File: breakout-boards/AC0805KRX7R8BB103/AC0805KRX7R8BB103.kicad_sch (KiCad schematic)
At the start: 0 parts

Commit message: feat: create schematic for 10nf breakout board
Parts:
- added C1, C10, C11, C12, C2, C3, C4, C5, C6, C7, C8, C9: 10nF, CAPC2012X95N, symbol FixedWing:AC0805KRX7R8BB103
- added TP1, TP10, TP11, TP12, TP13, TP14, TP15, TP16, TP17, TP18, TP19, TP2, TP20, TP21, TP22, TP23, TP24, TP3, TP4, TP5, TP6, TP7, TP8, TP9: TestPoint, symbol Connector:TestPoint
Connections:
- new net: C9.2, TP21.1
- new net: C12.1, TP12.1
- new net: C6.2, TP18.1
- new net: C7.2, TP19.1
- new net: C6.1, TP6.1
- new net: C5.1, TP5.1
- new net: C5.2, TP17.1
- new net: C7.1, TP7.1
- new net: C11.2, TP23.1
- new net: C12.2, TP24.1
- new net: C4.1, TP4.1
- new net: C4.2, TP16.1
- new net: C10.2, TP22.1
- new net: C10.1, TP10.1
- new net: C2.1, TP2.1
- new net: C2.2, TP14.1
- new net: C1.2, TP13.1
- new net: C3.2, TP15.1
- new net: C1.1, TP1.1
- new net: C9.1, TP9.1
- new net: C11.1, TP11.1
- new net: C3.1, TP3.1
- new net: C8.1, TP8.1
- new net: C8.2, TP20.1

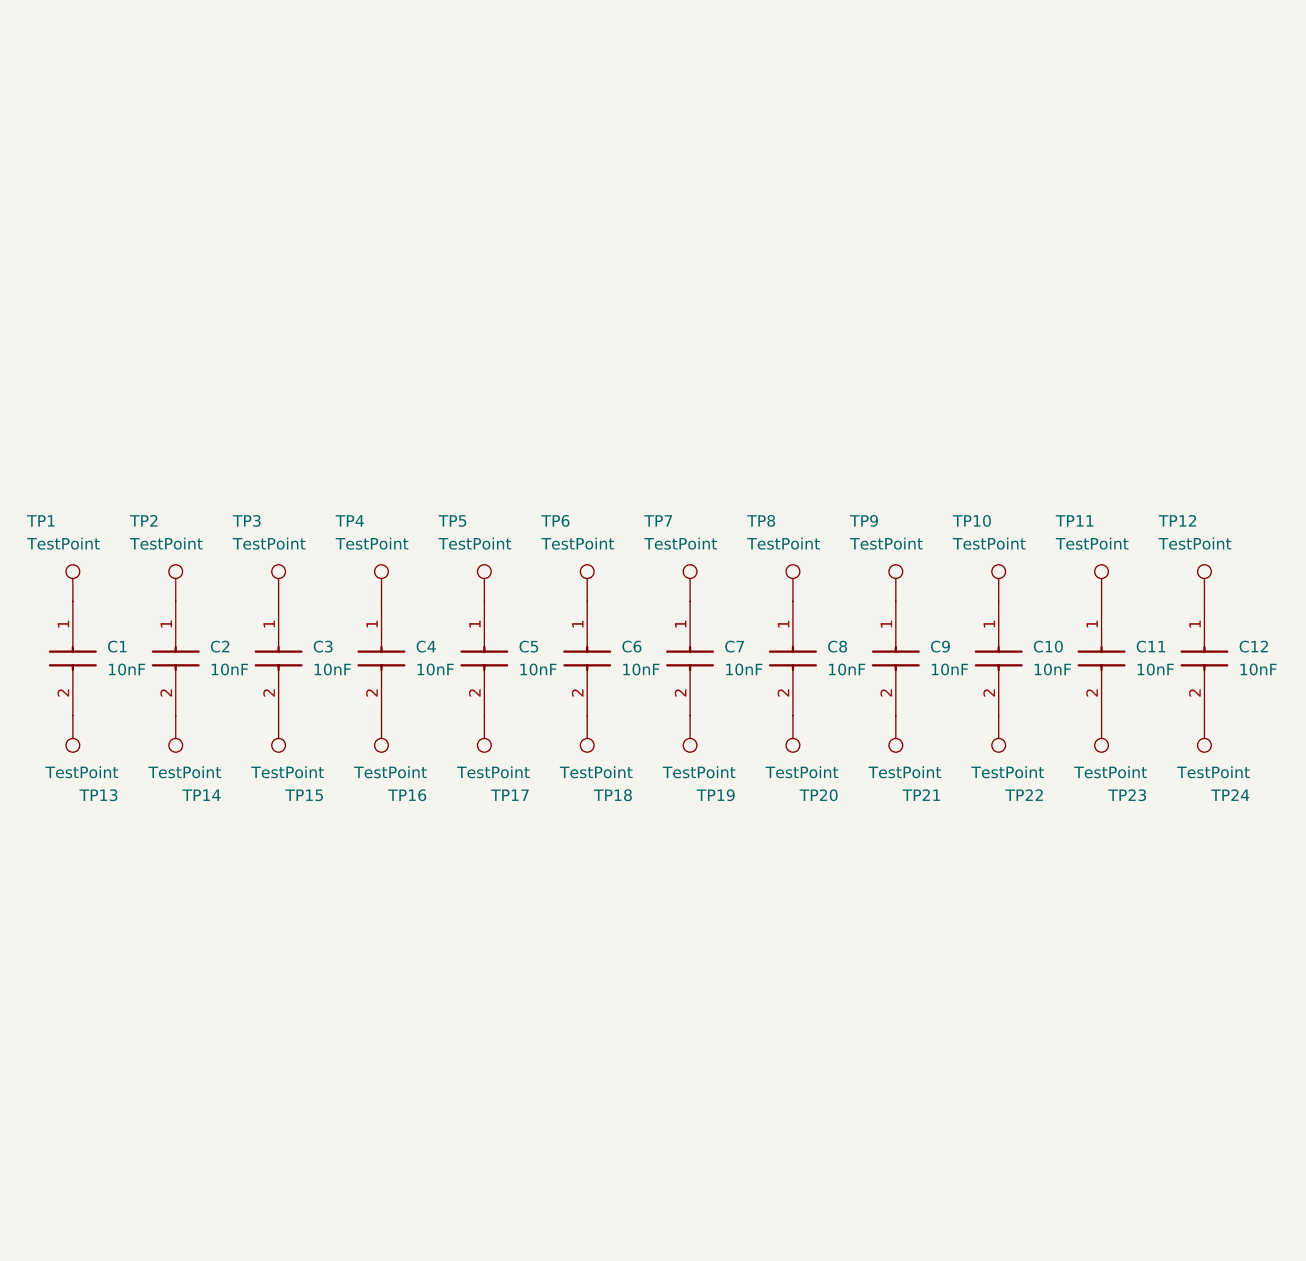
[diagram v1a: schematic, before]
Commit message: feat: add capacitor breakout board
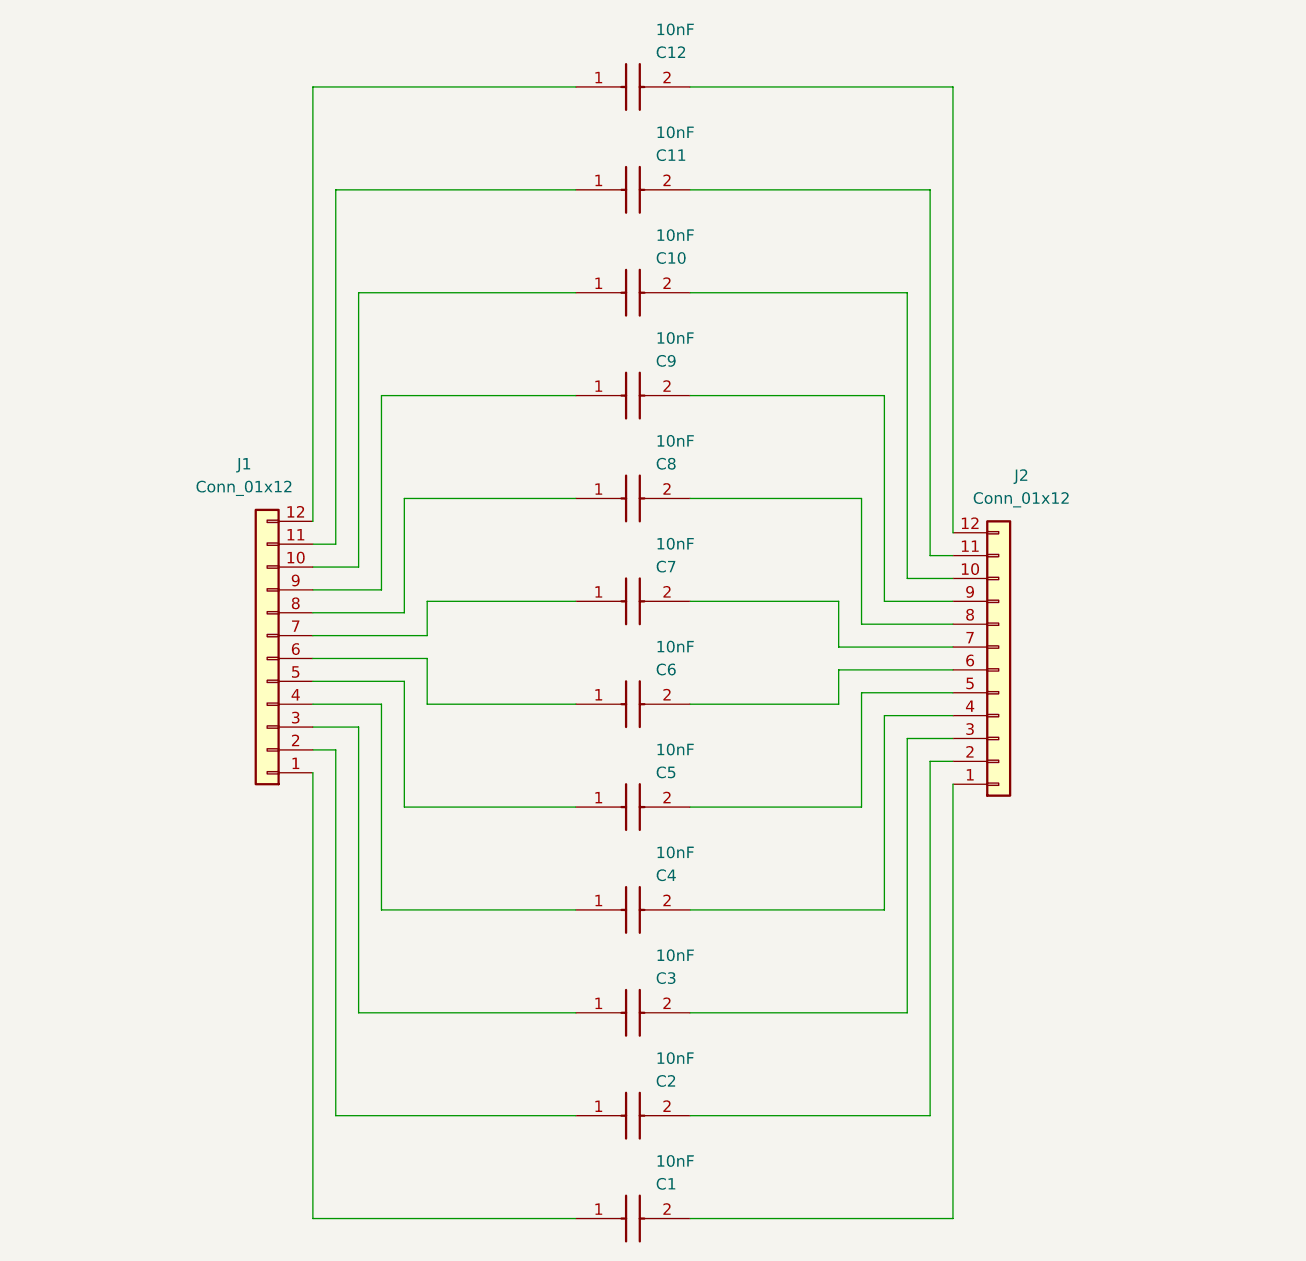
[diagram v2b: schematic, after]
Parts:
- removed TP1, TP10, TP11, TP12, TP13, TP14, TP15, TP16, TP17, TP18, TP19, TP2, TP20, TP21, TP22, TP23, TP24, TP3, TP4, TP5, TP6, TP7, TP8, TP9: TestPoint, symbol Connector:TestPoint
- added J1, J2: Conn_01x12, Connector_PinSocket_2.54mm:PinSocket_1x12_P2.54mm_Vertical, symbol Connector_Generic:Conn_01x12
- C1, C10, C11, C12, C2, C3, C4, C5, C6, C7, C8, C9: footprint CAPC2012X95N -> FixedWing:CAPC2012X95N
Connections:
- net at C9.2: now also J2.9 (Pin_9)
- net at C12.1: now also J1.12 (Pin_12)
- net at C6.2: now also J2.6 (Pin_6)
- net at C7.2: now also J2.7 (Pin_7)
- net at C6.1: now also J1.6 (Pin_6)
- net at C5.1: now also J1.5 (Pin_5)
- net at C5.2: now also J2.5 (Pin_5)
- net at C7.1: now also J1.7 (Pin_7)
- net at C11.2: now also J2.11 (Pin_11)
- net at C12.2: now also J2.12 (Pin_12)
- net at C4.1: now also J1.4 (Pin_4)
- net at C4.2: now also J2.4 (Pin_4)
- net at C10.2: now also J2.10 (Pin_10)
- net at C10.1: now also J1.10 (Pin_10)
- net at C2.1: now also J1.2 (Pin_2)
- net at C2.2: now also J2.2 (Pin_2)
- net at C1.2: now also J2.1 (Pin_1)
- net at C3.2: now also J2.3 (Pin_3)
- net at C1.1: now also J1.1 (Pin_1)
- net at C9.1: now also J1.9 (Pin_9)
- net at C11.1: now also J1.11 (Pin_11)
- net at C3.1: now also J1.3 (Pin_3)
- net at C8.1: now also J1.8 (Pin_8)
- net at C8.2: now also J2.8 (Pin_8)
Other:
- moved on the sheet: C1, C10, C11, C12, C2, C3, C4, C5, C6, C7, C8, C9

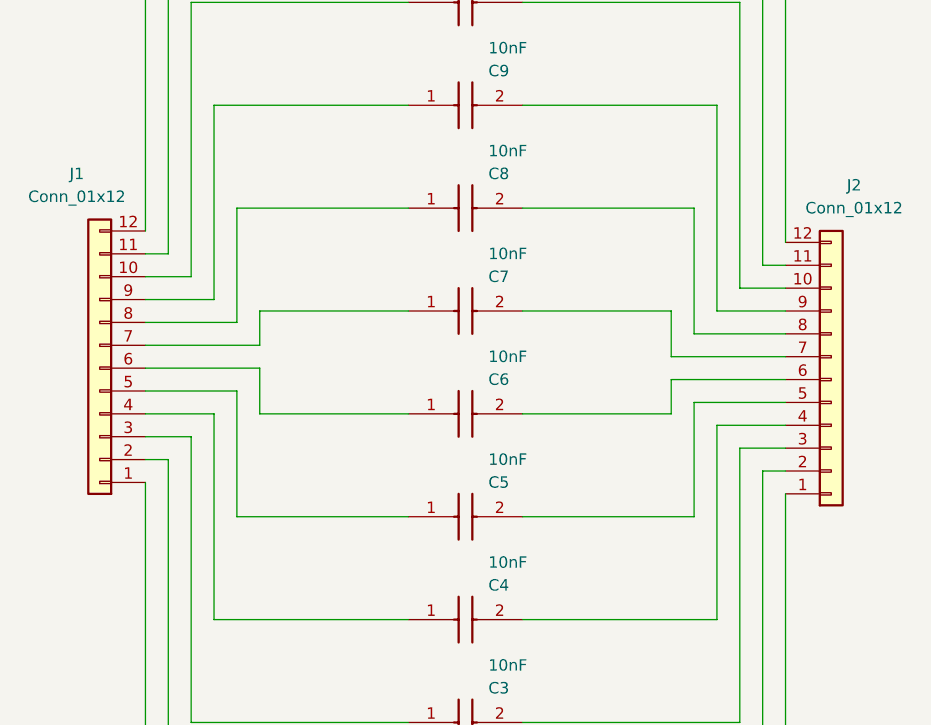
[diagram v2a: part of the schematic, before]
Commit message: feat: create footprint for capacitor breakout board
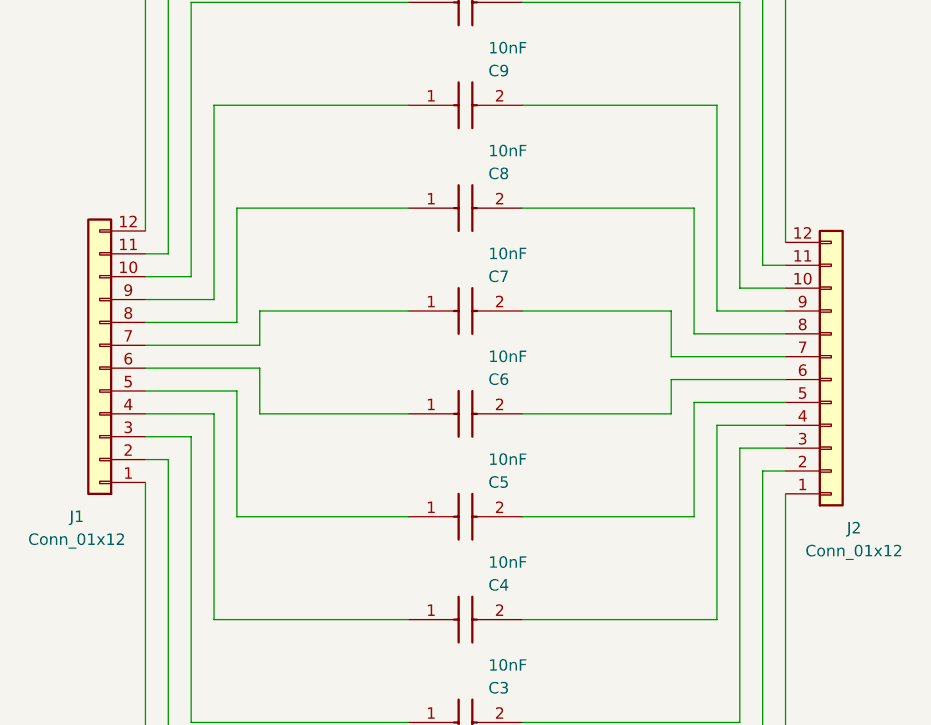
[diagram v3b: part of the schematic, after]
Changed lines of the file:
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@@
   (symbol (lib_id "Connector_Generic:Conn_01x12") (at 190.5 100.33 0) (mirror x) (unit 1)
     (in_bom yes) (on_board yes) (dnp no)
-    (property "Reference" "J2" (at 193.04 78.74 0)
+    (property "Reference" "J2" (at 193.04 116.84 0)
       (effects (font (size 1.27 1.27)))
     )
-    (property "Value" "Conn_01x12" (at 193.04 81.28 0)
+    (property "Value" "Conn_01x12" (at 193.04 119.38 0)
       (effects (font (size 1.27 1.27)))
     )
@@
   (symbol (lib_id "Connector_Generic:Conn_01x12") (at 109.22 99.06 180) (unit 1)
     (in_bom yes) (on_board yes) (dnp no)
-    (property "Reference" "J1" (at 106.68 77.47 0)
+    (property "Reference" "J1" (at 106.68 115.57 0)
       (effects (font (size 1.27 1.27)))
     )
-    (property "Value" "Conn_01x12" (at 106.68 80.01 0)
+    (property "Value" "Conn_01x12" (at 106.68 118.11 0)
       (effects (font (size 1.27 1.27)))
     )
